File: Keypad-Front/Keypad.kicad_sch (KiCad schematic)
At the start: 99 parts, among them J1 RTC STEMMA QT, J6 EXP QWIIC, J7 TOUCH QWIIC, U1 DS3231MZ, U2 PCA9536DP, U3 CAP1214, U4 PN5321A3HN_C1xx, U5 MCP9808_MSOP, Y3 27.12MHz

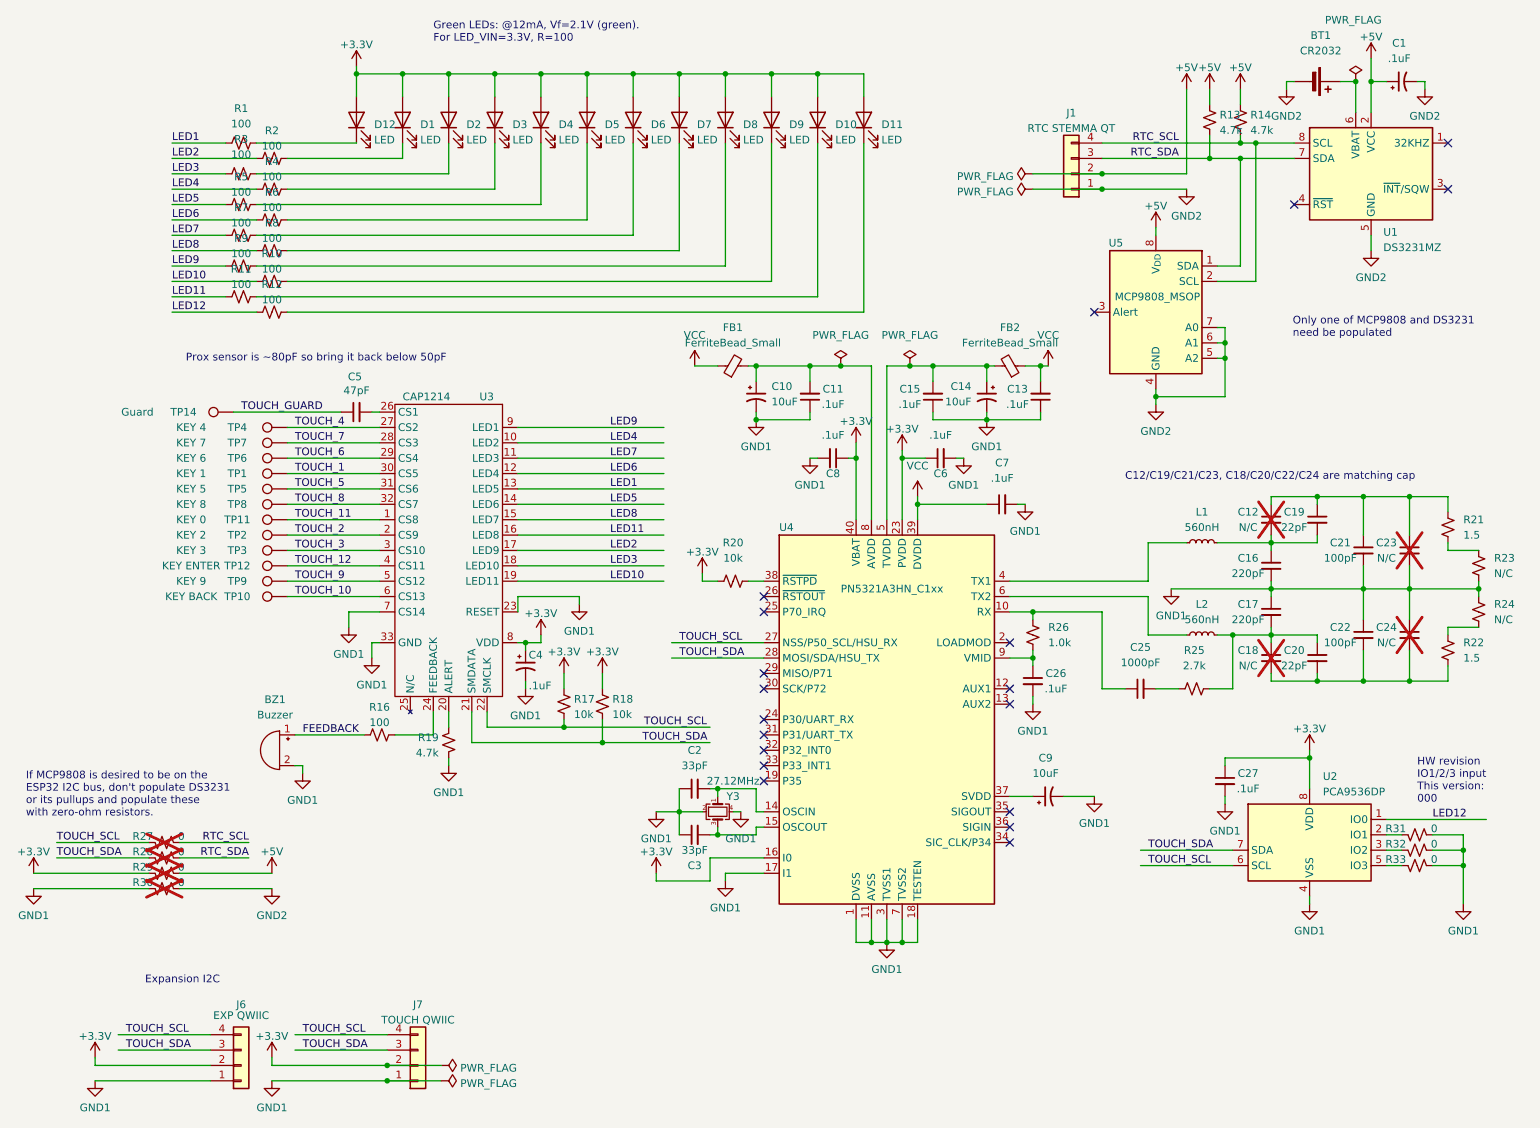
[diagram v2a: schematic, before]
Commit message: More work on schematic and gerbers; fill out BOM with JLCPCB part #s
Also updated the README a bit.
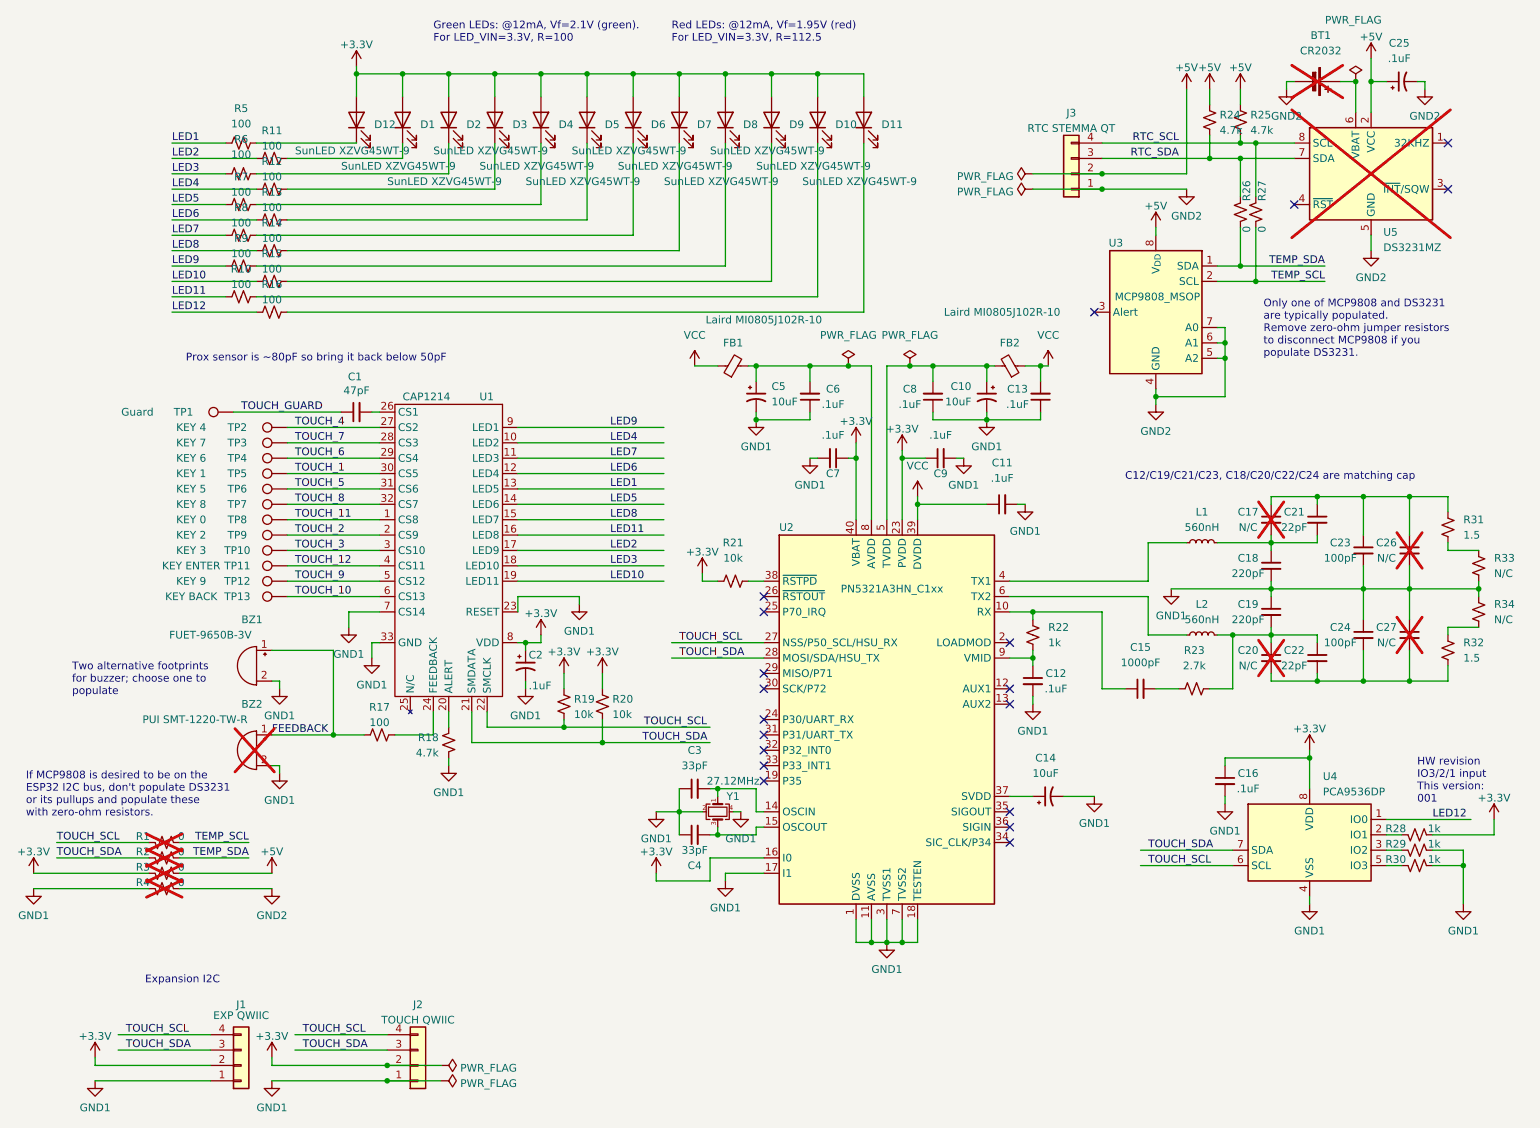
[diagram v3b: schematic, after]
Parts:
- added BZ1: FUET-9650B-3V, Keypad:FUET-9650B-3V, symbol Device:Buzzer
- added R26, R27: 0, Resistor_SMD:R_0805_2012Metric_Pad1.20x1.40mm_HandSolder, symbol Device:R_Small_US
- BT1: Digikey (none) -> BC-2003-TR-CT-ND; LCSC (none) -> C7085256; now not fitted
- BZ2: renamed from BZ1; value Buzzer -> PUI SMT-1220-TW-R; Digikey (none) -> 668-1086-ND; now not fitted
- C1: renamed from C5; LCSC (none) -> C14857
- C10: renamed from C14; LCSC (none) -> C15850
- C11: renamed from C7; LCSC (none) -> C49678
- C12: renamed from C26; LCSC (none) -> C49678
- C13: LCSC (none) -> C49678
- C14: renamed from C9; LCSC (none) -> C15850
- C15: renamed from C25; Digikey (none) -> 399-C0805C102J5GAC7210CT-ND; LCSC (none) -> C46653
- C16: renamed from C27; LCSC (none) -> C49678
- C18: renamed from C16; LCSC (none) -> C107145
- C19: renamed from C17; LCSC (none) -> C107145
- C2: renamed from C4; LCSC (none) -> C49678
- C21: renamed from C19; LCSC (none) -> C1804
- C22: renamed from C20; LCSC (none) -> C1804
- C23: renamed from C21; Digikey (none) -> 399-C0805C101J5GAC7210CT-ND; LCSC (none) -> C1790
- C24: renamed from C22; Digikey (none) -> 399-C0805C101J5GAC7210CT-ND; LCSC (none) -> C1790
- C25: renamed from C1; LCSC (none) -> C49678
- C3: renamed from C2; footprint Capacitor_SMD:C_0805_2012Metric_Pad1.18x1.45mm_HandSolder -> Capacitor_SMD:C_0603_1608Metric_Pad1.08x0.95mm_HandSolder; LCSC (none) -> C1663
- C4: renamed from C3; footprint Capacitor_SMD:C_0805_2012Metric_Pad1.18x1.45mm_HandSolder -> Capacitor_SMD:C_0603_1608Metric_Pad1.08x0.95mm_HandSolder; LCSC (none) -> C1663
- C5: renamed from C10; LCSC (none) -> C15850
- C6: renamed from C11; LCSC (none) -> C49678
- C7: renamed from C8; LCSC (none) -> C49678
- C8: renamed from C15; LCSC (none) -> C49678
- C9: renamed from C6; LCSC (none) -> C49678
- D1, D10, D11, D12, D2, D3, D4, D5, D6, D7, D8, D9: value LED -> SunLED XZVG45WT-9; Digikey (none) -> 1497-1336-1-ND; LCSC (none) -> C5838480
- FB1, FB2: value FerriteBead_Small -> Laird MI0805J102R-10; Digikey (none) -> 240-2551-1-ND; LCSC (none) -> C2441372
- J1: renamed from J6; LCSC (none) -> C160390
- J2: renamed from J7; LCSC (none) -> C160390
- J3: renamed from J1; LCSC (none) -> C160390
- L1, L2: Digikey (none) -> 553-BWCS00231715R56J00CT-ND; LCSC (none) -> C304279
- R1: renamed from R27; LCSC (none) -> C17477
- R10: renamed from R11; LCSC (none) -> C17802
- R11: renamed from R2; LCSC (none) -> C17802
- R12: renamed from R4; LCSC (none) -> C17802
- R13: renamed from R6; LCSC (none) -> C17802
- R14: renamed from R8; LCSC (none) -> C17802
- R15: renamed from R10; LCSC (none) -> C17802
- R16: renamed from R12; LCSC (none) -> C17802
- R17: renamed from R16; LCSC (none) -> C17802
- R18: renamed from R19; LCSC (none) -> C17673
- R19: renamed from R17; LCSC (none) -> C17414
- R2: renamed from R28; LCSC (none) -> C17477
- R20: renamed from R18; LCSC (none) -> C17414
- R21: renamed from R20; LCSC (none) -> C17414
- R22: renamed from R26; value 1.0k -> 1k; LCSC (none) -> C17513
- R23: renamed from R25; LCSC (none) -> C17530
- R24: renamed from R13; LCSC (none) -> C17673
- R25: renamed from R14; LCSC (none) -> C17673
- R28: renamed from R31; value 0 -> 1k; LCSC (none) -> C17513
- R29: renamed from R32; value 0 -> 1k; LCSC (none) -> C17513
- R3: renamed from R29; LCSC (none) -> C17477
- R30: renamed from R33; value 0 -> 1k; LCSC (none) -> C17513
- R31: renamed from R21; LCSC (none) -> C17392
- R32: renamed from R22; LCSC (none) -> C17392
- R33: renamed from R23; now left out of the parts list
- R34: renamed from R24; now left out of the parts list
- R4: renamed from R30; LCSC (none) -> C17477
- R5: renamed from R1; LCSC (none) -> C17802
- R6: renamed from R3; LCSC (none) -> C17802
- R7: renamed from R5; LCSC (none) -> C17802
- R8: renamed from R7; LCSC (none) -> C17802
- R9: LCSC (none) -> C17802
- TP1: renamed from TP14; now left out of the parts list
- TP10: renamed from TP3; now left out of the parts list
- TP11: renamed from TP12; now left out of the parts list
- TP12: renamed from TP9; now left out of the parts list
- TP13: renamed from TP10; now left out of the parts list
- TP2: renamed from TP4; now left out of the parts list
- TP3: renamed from TP7; now left out of the parts list
- TP4: renamed from TP6; now left out of the parts list
- TP5: renamed from TP1; now left out of the parts list
- TP6: renamed from TP5; now left out of the parts list
- TP7: renamed from TP8; now left out of the parts list
- TP8: renamed from TP11; now left out of the parts list
- TP9: renamed from TP2; now left out of the parts list
- U1: renamed from U3; Digikey (none) -> CAP1214-1-EZK-TRCT-ND; LCSC (none) -> C2652059
- U2: renamed from U4; Digikey (none) -> 568-13228-ND; LCSC (none) -> C880904
- U3: renamed from U5; Digikey (none) -> MCP9808T-E/MSCT-ND; LCSC (none) -> C94847
- U4: renamed from U2; Digikey (none) -> 568-1836-1-ND; LCSC (none) -> C14674
- U5: renamed from U1; Digikey (none) -> DS3231MZ+-ND; LCSC (none) -> C107410; now not fitted
- Y1: renamed from Y3; Digikey (none) -> 887-1424-1-ND; LCSC (none) -> C70591
- renumbered C12 to C17, C18 to C20, C23 to C26, C24 to C27
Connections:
- net +3.3V: now also R28.2
- net FEEDBACK: now also BZ1.1 (+)
- net GND1: now also BZ1.2 (-); no longer R28.2
- net RTC_SCL: now also R27.1; no longer R1.2, U3.2 (SCL)
- net RTC_SDA: now also R26.1; no longer R2.2, U3.1 (SDA)
- new net TEMP_SCL: R1.2, R27.2, U3.2 (SCL)
- new net TEMP_SDA: R2.2, R26.2, U3.1 (SDA)
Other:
- note added: "HW revision IO3/2/1 input This version: 001"
- note added: "Only one of MCP9808 and DS3231 are typically populated. Remove zero-ohm jumper resistors to disconnect MCP9808 if you populate DS3231."
- note added: "Red LEDs: @12mA, Vf=1.95V (red) For LED_VIN=3.3V, R=112.5"
- note added: "Two alternative footprints for buzzer; choose one to populate"
- note removed: "HW revision IO1/2/3 input This version: 000"
- note removed: "Only one of MCP9808 and DS3231 need be populated"

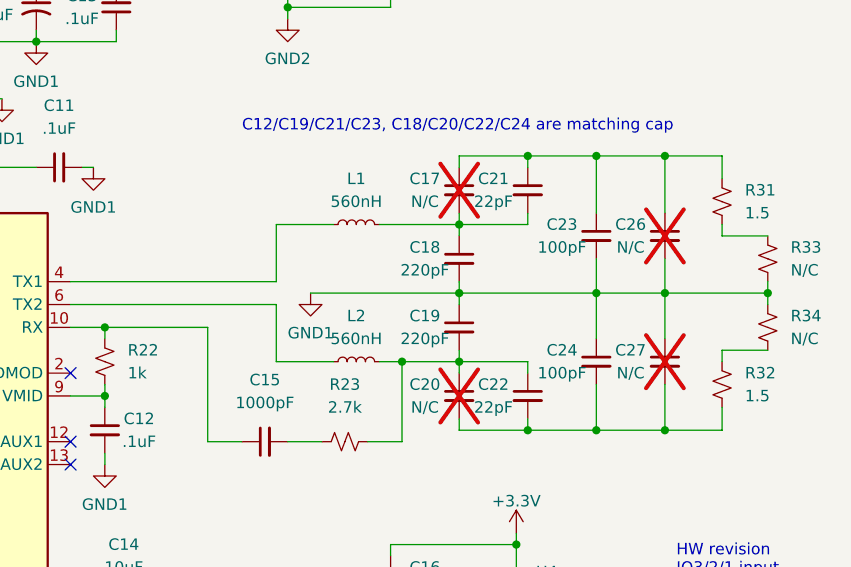
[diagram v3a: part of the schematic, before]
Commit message: RFID tuning
Tuned the length of the TX1 and TX2 traces to maintain symmetry; moved
L1/L2 around a bit to the same end.  Added a zero-ohm resistor so we
can disconnect the antenna "virtual ground" from the actual ground,
as recommended by the AN1445 app note.
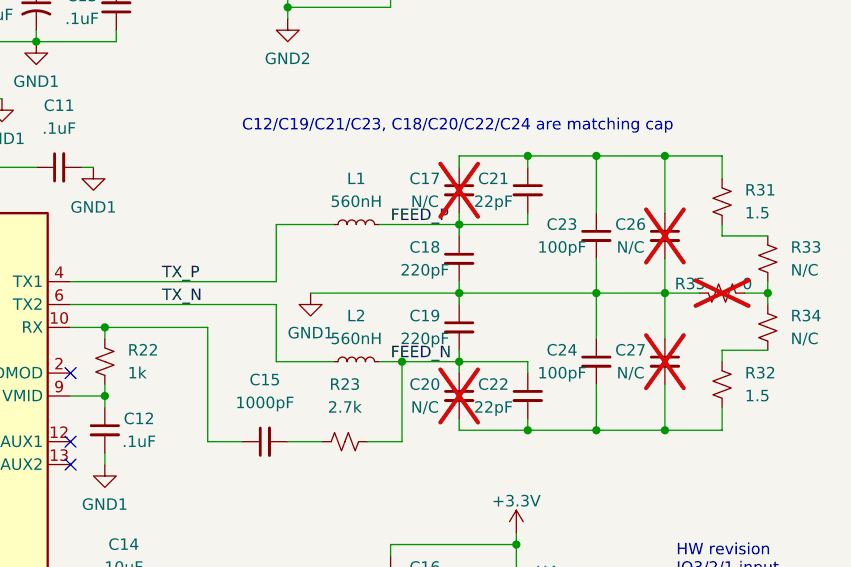
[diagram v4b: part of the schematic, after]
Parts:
- added R35: 0, Resistor_SMD:R_0402_1005Metric, symbol Device:R_Small_US
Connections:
- net GND1: now also R35.1; no longer R33.1, R34.2
- net TX_P: now reaches L1.1, U2.4 (TX1)
- net TX_N: now reaches L2.1, U2.6 (TX2)
- net FEED_N: now reaches C19.2, C20.1, C22.1, L2.2, R23.1
- net FEED_P: now reaches C17.2, C18.1, C21.2, L1.2
- new net: R33.1, R34.2, R35.2
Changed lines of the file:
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@@
   (junction (at 179.07 82.55) (diameter 0) (color 0 0 0 0)
   )
-  (junction (at 260.35 110.49) (diameter 0) (color 0 0 0 0)
-  )
   (junction (at 241.3 125.73) (diameter 0) (color 0 0 0 0)
   )
@@
   (junction (at 220.98 36.83) (diameter 0) (color 0 0 0 0)
   )
+  (junction (at 260.35 110.49) (diameter 0) (color 0 0 0 0)
+  )
   (junction (at 167.64 96.52) (diameter 0) (color 0 0 0 0)
   )
@@
     (stroke (width 0) (type default))
   )
+  (wire (pts (xy 260.35 110.49) (xy 260.35 111.76))
+    (stroke (width 0) (type default))
+  )
   (wire (pts (xy 255.27 123.19) (xy 255.27 125.73))
     (stroke (width 0) (type default))
@@
     (stroke (width 0) (type default))
   )
+  (wire (pts (xy 257.81 110.49) (xy 260.35 110.49))
+    (stroke (width 0) (type default))
+  )
   (wire (pts (xy 187.96 76.2) (xy 187.96 73.66))
     (stroke (width 0) (type default))
@@
     (stroke (width 0) (type default))
   )
-  (wire (pts (xy 260.35 110.49) (xy 260.35 111.76))
+  (wire (pts (xy 260.35 109.22) (xy 260.35 110.49))
     (stroke (width 0) (type default))
   )
@@
     (stroke (width 0) (type default))
   )
+  (wire (pts (xy 248.92 110.49) (xy 252.73 110.49))
+    (stroke (width 0) (type default))
+  )
   (wire (pts (xy 81.28 134.62) (xy 87.63 134.62))
     (stroke (width 0) (type default))
@@
     (stroke (width 0) (type default))
   )
-  (wire (pts (xy 260.35 110.49) (xy 248.92 110.49))
-    (stroke (width 0) (type default))
-  )
   (wire (pts (xy 205.74 109.22) (xy 205.74 102.87))
     (stroke (width 0) (type default))
@@
     (stroke (width 0) (type default))
   )
-  (wire (pts (xy 260.35 109.22) (xy 260.35 110.49))
-    (stroke (width 0) (type default))
-  )
   (wire (pts (xy 165.1 87.63) (xy 165.1 88.9))
     (stroke (width 0) (type default))
@@
     (effects (font (size 1.27 1.27)) (justify right bottom))
   )
+  (label "FEED_P" (at 218.44 102.87 0) (fields_autoplaced)
+    (effects (font (size 1.27 1.27)) (justify left bottom))
+  )
   (label "TOUCH_1" (at 64.77 91.44 0) (fields_autoplaced)
     (effects (font (size 1.27 1.27)) (justify left bottom))
@@
     (effects (font (size 1.27 1.27)) (justify left bottom))
   )
+  (label "TX_P" (at 193.04 109.22 0) (fields_autoplaced)
+    (effects (font (size 1.27 1.27)) (justify left bottom))
+  )
   (label "LED9" (at 116.84 83.82 0) (fields_autoplaced)
     (effects (font (size 1.27 1.27)) (justify left bottom))
@@
     (effects (font (size 1.27 1.27)) (justify left bottom))
   )
+  (label "FEED_N" (at 218.44 118.11 0) (fields_autoplaced)
+    (effects (font (size 1.27 1.27)) (justify left bottom))
+  )
   (label "LED5" (at 116.84 96.52 0) (fields_autoplaced)
     (effects (font (size 1.27 1.27)) (justify left bottom))
   )
+  (label "TX_N" (at 193.04 111.76 0) (fields_autoplaced)
+    (effects (font (size 1.27 1.27)) (justify left bottom))
+  )
   (label "TOUCH_SDA" (at 66.04 186.69 0) (fields_autoplaced)
     (effects (font (size 1.27 1.27)) (justify left bottom))
@@
         )
       )
+    )
+  )
+  (symbol (lib_id "Device:R_Small_US") (at 255.27 110.49 90) (mirror x) (unit 1)
+    (in_bom yes) (on_board yes) (dnp yes)
+    (property "Reference" "R35" (at 251.7277 109.4649 90)
+      (effects (font (size 1.27 1.27)))
+    )
+    (property "Value" "0" (at 258.0777 109.4649 90)
+      (effects (font (size 1.27 1.27)))
+    )
+    (property "Footprint" "Resistor_SMD:R_0402_1005Metric" (at 255.27 110.49 0)
+      (effects (font (size 1.27 1.27)) hide)
+    )
+    (property "Datasheet" "~" (at 255.27 110.49 0)
+      (effects (font (size 1.27 1.27)) hide)
+    )
+    (property "Digikey" "" (at 255.27 110.49 0)
+      (effects (font (size 1.27 1.27)) hide)
+    )
+    (property "LCSC" "C17477" (at 255.27 110.49 0)
+      (effects (font (size 1.27 1.27)) hide)
+    )
+    (pin "1")
+    (pin "2")
+    (instances
+      (project "Keypad"
+        (path "/ed47ce54-8b56-4a78-a942-9443bc7041ac"
+          (reference "R35") (unit 1)
+        )
+      )
